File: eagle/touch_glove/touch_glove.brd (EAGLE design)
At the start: 160 x 100 mm, 0 parts

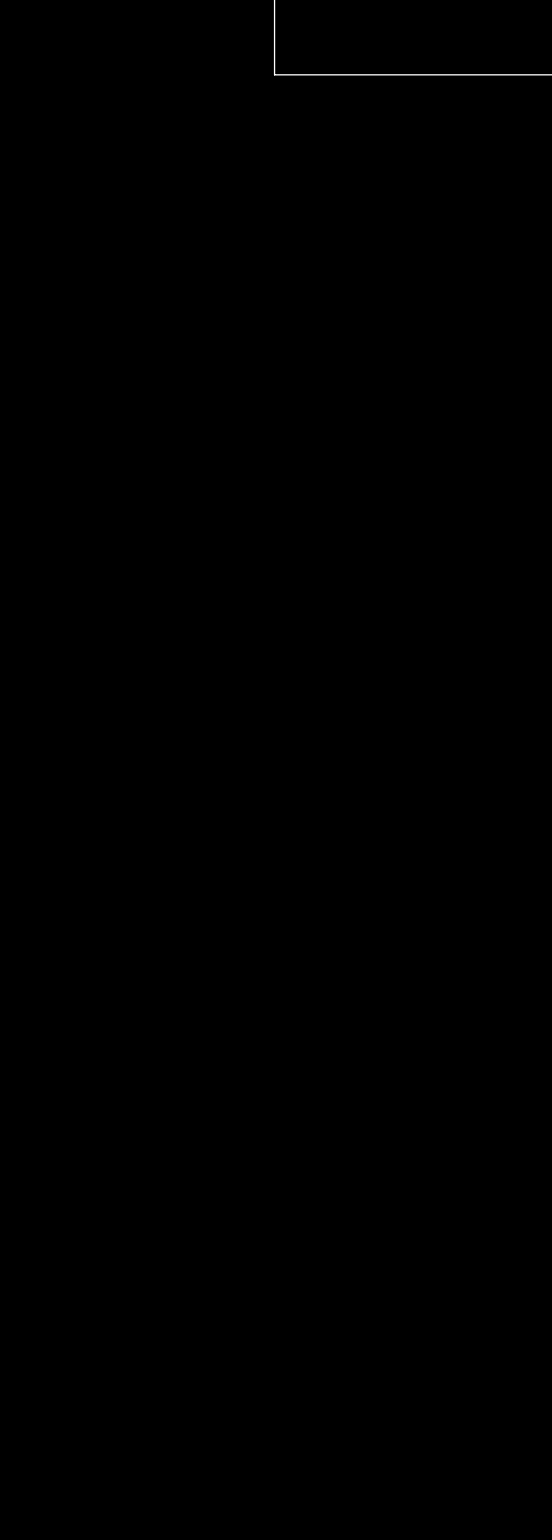
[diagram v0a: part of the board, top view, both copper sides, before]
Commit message: Added PWM driver and DEMUX to both robotic arm and touch glove.  Added some transistors to touch glove
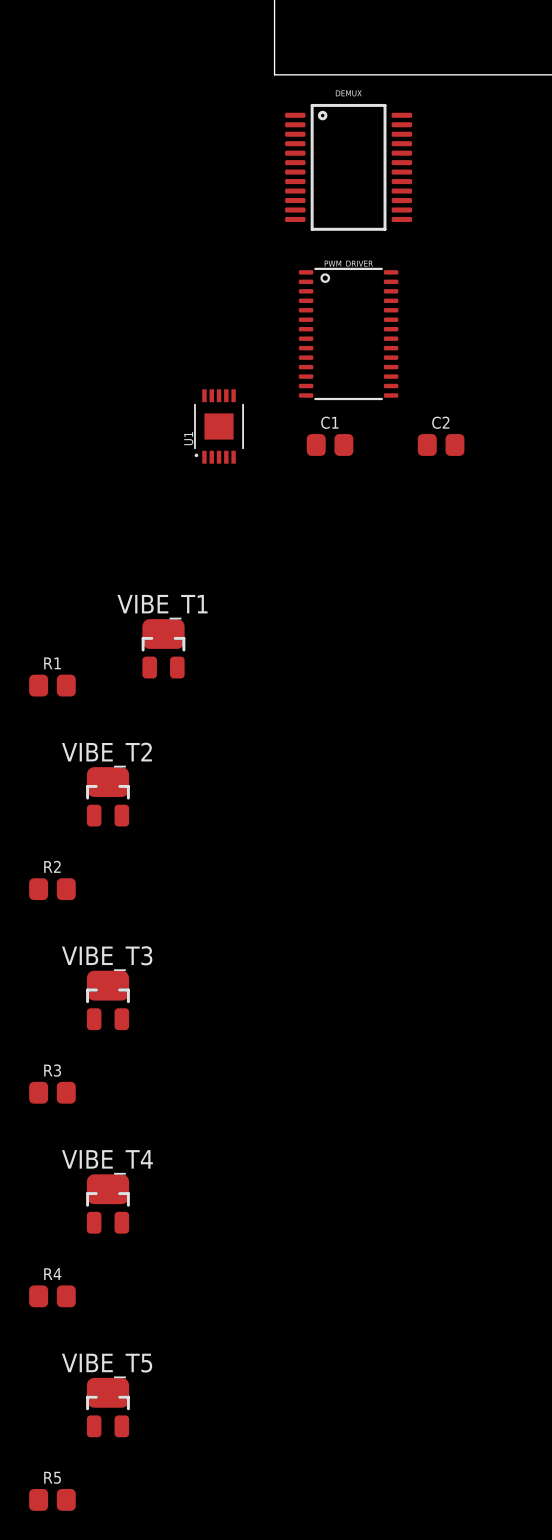
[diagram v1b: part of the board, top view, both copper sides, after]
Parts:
- added C1: CAP_CER_SMD-805_0.1UF-50V-10%, MrSwirlyEyes:CAP_CER_SMD-805_0.1UF-50V-10%
- added C2: CAP_CER_SMD-805_10UF-25V-10%, MrSwirlyEyes:CAP_CER_SMD-805_10UF-25V-10%
- added DEMUX: CD74HC4067-SM96_16:1_MUX-DEMUX, MrSwirlyEyes:SSOP24
- added PWM_DRIVER: PCA9685_16-CH_12-BIT_PWM-DRIVER, MrSwirlyEyes:TSSOP28
- added R1, R2, R3, R4, R5: RES_SMD-805_10K-5%-1/8W, MrSwirlyEyes:RES_SMD-805_10K-5%-1/8W
- added U1: DRV8830, SparkFun-Retired:MSOP-10-GNDPAD
- added VIBE_T1, VIBE_T2, VIBE_T3, VIBE_T4, VIBE_T5: SI2302CDS-MOSFET-N-CH_2.6A_20V_57MΩ_SOT23-3, MrSwirlyEyes:SOT23-3
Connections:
- new net C10: DEMUX.21
- new net C11: DEMUX.20
- new net C12: DEMUX.19
- new net C13: DEMUX.18
- new net C14: DEMUX.17
- new net C15: DEMUX.16
- new net C5: DEMUX.4
- new net C6: DEMUX.3
- new net C7: DEMUX.2
- new net C8: DEMUX.23
- new net C9: DEMUX.22
- new net GND: C1.2, C2.2, DEMUX.12, DEMUX.15, PWM_DRIVER.1, PWM_DRIVER.14, PWM_DRIVER.2, PWM_DRIVER.23, PWM_DRIVER.24, PWM_DRIVER.25, PWM_DRIVER.3, PWM_DRIVER.4, PWM_DRIVER.5, R1.1, R2.1, R3.1, R4.1, R5.1, U1.5, VIBE_T1.S, VIBE_T2.S, VIBE_T3.S, VIBE_T4.S, VIBE_T5.S
- new net OUT1: U1.3
- new net OUT2: U1.1
- new net PPAD: U1.GND
- new net PWM10: PWM_DRIVER.17
- new net S0: DEMUX.10
- new net S1: DEMUX.11
- new net S2: DEMUX.14
- new net S3: DEMUX.13
- new net SCL: PWM_DRIVER.26
- new net SDA: PWM_DRIVER.27
- new net SIG: DEMUX.1
- new net STRAIN_1: DEMUX.9
- new net STRAIN_2: DEMUX.8
- new net STRAIN_3: DEMUX.7
- new net STRAIN_4: DEMUX.6
- new net STRAIN_5: DEMUX.5
- new net TEC_1_COLD: PWM_DRIVER.7
- new net TEC_1_HOT: PWM_DRIVER.6
- new net TEC_2_COLD: PWM_DRIVER.9
- new net TEC_2_HOT: PWM_DRIVER.8
- new net TEC_3_COLD: PWM_DRIVER.11
- new net TEC_3_HOT: PWM_DRIVER.10
- new net TEC_4_COLD: PWM_DRIVER.13
- new net TEC_4_HOT: PWM_DRIVER.12
- new net TEC_5_COLD: PWM_DRIVER.16
- new net TEC_5_HOT: PWM_DRIVER.15
- new net VCC: C1.1, C2.1, DEMUX.24, PWM_DRIVER.28, U1.4, VIBE_T1.D, VIBE_T2.D, VIBE_T3.D, VIBE_T4.D, VIBE_T5.D
- new net VIBE_1: PWM_DRIVER.18, R1.2, VIBE_T1.G
- new net VIBE_2: PWM_DRIVER.19, R2.2, VIBE_T2.G
- new net VIBE_3: PWM_DRIVER.20, R3.2, VIBE_T3.G
- new net VIBE_4: PWM_DRIVER.21, R4.2, VIBE_T4.G
- new net VIBE_5: PWM_DRIVER.22, R5.2, VIBE_T5.G

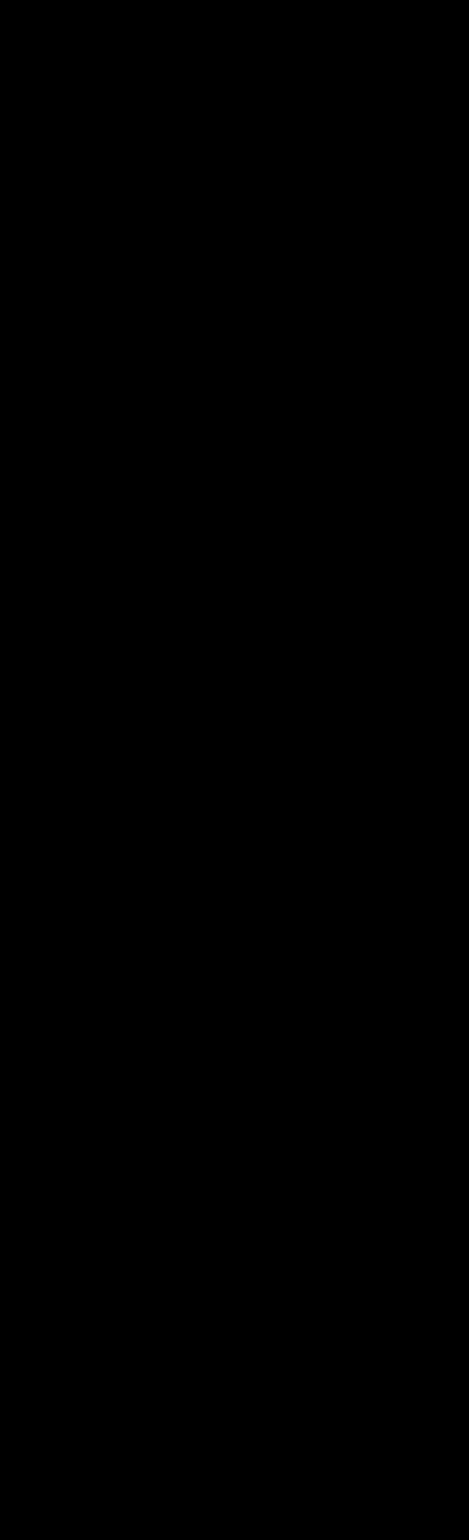
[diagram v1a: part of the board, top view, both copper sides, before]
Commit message: Added vibe motor plus transistor driver arrangement
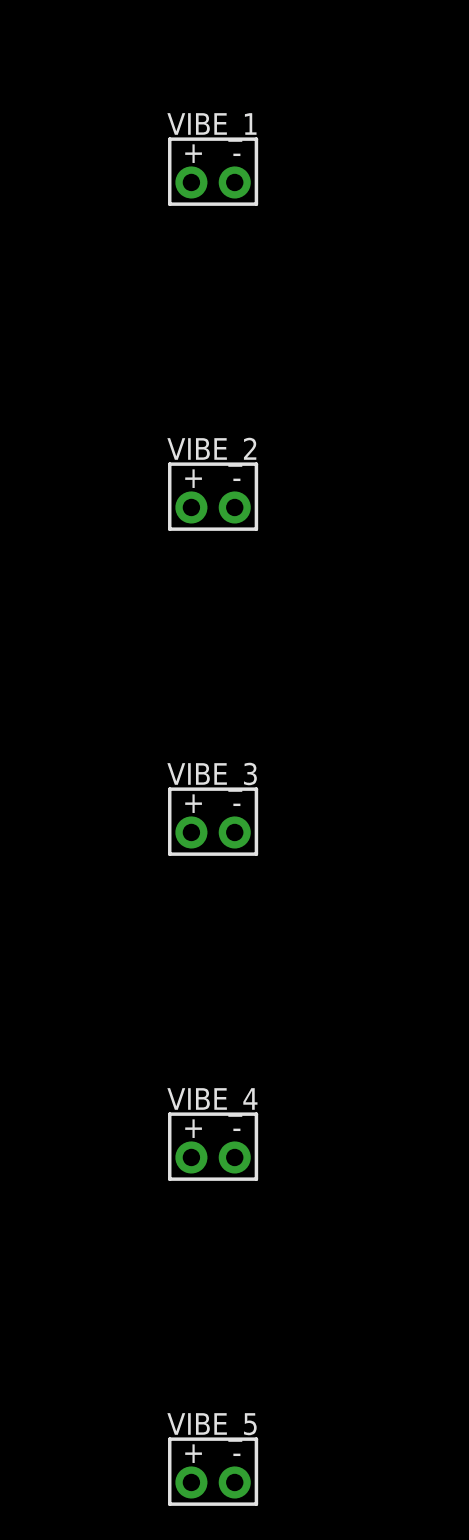
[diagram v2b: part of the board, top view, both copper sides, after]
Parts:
- added VIBE_1, VIBE_2, VIBE_3, VIBE_4, VIBE_5: VIBE_MOTOR, MrSwirlyEyes:CONNECTOR-01X02
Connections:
- new net N$1: VIBE_1.2, VIBE_T1.D
- new net N$2: VIBE_5.2, VIBE_T5.D
- new net N$3: VIBE_4.2, VIBE_T4.D
- new net N$4: VIBE_3.2, VIBE_T3.D
- new net N$5: VIBE_2.2, VIBE_T2.D
- net VCC: now also VIBE_1.1, VIBE_2.1, VIBE_3.1, VIBE_4.1, VIBE_5.1; no longer VIBE_T1.D, VIBE_T2.D, VIBE_T3.D, VIBE_T4.D, VIBE_T5.D
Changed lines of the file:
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@@
 <attribute name="TESTED" value="NO" x="-20.32" y="-92.71" size="1.778" layer="27" display="off"/>
+</element>
+<element name="VIBE_1" library="MrSwirlyEyes" package="CONNECTOR-01X02" value="VIBE_MOTOR" x="-6.35" y="-109.22">
+<attribute name="CREATOR" value="MrSwirlyEyes" x="-6.35" y="-109.22" size="1.778" layer="27" display="off"/>
+<attribute name="DATASHEET" value="http://www.vibration-motor.com/products/download/C0825B002F.pdf" x="-6.35" y="-109.22" size="1.778" layer="27" display="off"/>
+<attribute name="DIST" value="Digikey" x="-6.35" y="-109.22" size="1.778" layer="27" display="off"/>
+<attribute name="DISTPN" value="1670-1002-ND" x="-6.35" y="-109.22" size="1.778" layer="27" display="off"/>
+<attribute name="MFR" value="Jinlong Machinery &amp; Electronics, Inc." x="-6.35" y="-109.22" size="1.778" layer="27" display="off"/>
+<attribute name="MPN" value="C0825B002F" x="-6.35" y="-109.22" size="1.778" layer="27" display="off"/>
+<attribute name="TESTED" value="NO" x="-6.35" y="-109.22" size="1.778" layer="27" display="off"/>
+</element>
+<element name="VIBE_2" library="MrSwirlyEyes" package="CONNECTOR-01X02" value="VIBE_MOTOR" x="-6.35" y="-128.27">
+<attribute name="CREATOR" value="MrSwirlyEyes" x="-6.35" y="-128.27" size="1.778" layer="27" display="off"/>
+<attribute name="DATASHEET" value="http://www.vibration-motor.com/products/download/C0825B002F.pdf" x="-6.35" y="-128.27" size="1.778" layer="27" display="off"/>
+<attribute name="DIST" value="Digikey" x="-6.35" y="-128.27" size="1.778" layer="27" display="off"/>
+<attribute name="DISTPN" value="1670-1002-ND" x="-6.35" y="-128.27" size="1.778" layer="27" display="off"/>
+<attribute name="MFR" value="Jinlong Machinery &amp; Electronics, Inc." x="-6.35" y="-128.27" size="1.778" layer="27" display="off"/>
+<attribute name="MPN" value="C0825B002F" x="-6.35" y="-128.27" size="1.778" layer="27" display="off"/>
+<attribute name="TESTED" value="NO" x="-6.35" y="-128.27" size="1.778" layer="27" display="off"/>
+</element>
+<element name="VIBE_3" library="MrSwirlyEyes" package="CONNECTOR-01X02" value="VIBE_MOTOR" x="-6.35" y="-147.32">
+<attribute name="CREATOR" value="MrSwirlyEyes" x="-6.35" y="-147.32" size="1.778" layer="27" display="off"/>
+<attribute name="DATASHEET" value="http://www.vibration-motor.com/products/download/C0825B002F.pdf" x="-6.35" y="-147.32" size="1.778" layer="27" display="off"/>
+<attribute name="DIST" value="Digikey" x="-6.35" y="-147.32" size="1.778" layer="27" display="off"/>
+<attribute name="DISTPN" value="1670-1002-ND" x="-6.35" y="-147.32" size="1.778" layer="27" display="off"/>
+<attribute name="MFR" value="Jinlong Machinery &amp; Electronics, Inc." x="-6.35" y="-147.32" size="1.778" layer="27" display="off"/>
+<attribute name="MPN" value="C0825B002F" x="-6.35" y="-147.32" size="1.778" layer="27" display="off"/>
+<attribute name="TESTED" value="NO" x="-6.35" y="-147.32" size="1.778" layer="27" display="off"/>
+</element>
+<element name="VIBE_4" library="MrSwirlyEyes" package="CONNECTOR-01X02" value="VIBE_MOTOR" x="-6.35" y="-166.37">
+<attribute name="CREATOR" value="MrSwirlyEyes" x="-6.35" y="-166.37" size="1.778" layer="27" display="off"/>
+<attribute name="DATASHEET" value="http://www.vibration-motor.com/products/download/C0825B002F.pdf" x="-6.35" y="-166.37" size="1.778" layer="27" display="off"/>
+<attribute name="DIST" value="Digikey" x="-6.35" y="-166.37" size="1.778" layer="27" display="off"/>
+<attribute name="DISTPN" value="1670-1002-ND" x="-6.35" y="-166.37" size="1.778" layer="27" display="off"/>
+<attribute name="MFR" value="Jinlong Machinery &amp; Electronics, Inc." x="-6.35" y="-166.37" size="1.778" layer="27" display="off"/>
+<attribute name="MPN" value="C0825B002F" x="-6.35" y="-166.37" size="1.778" layer="27" display="off"/>
+<attribute name="TESTED" value="NO" x="-6.35" y="-166.37" size="1.778" layer="27" display="off"/>
+</element>
+<element name="VIBE_5" library="MrSwirlyEyes" package="CONNECTOR-01X02" value="VIBE_MOTOR" x="-6.35" y="-185.42">
+<attribute name="CREATOR" value="MrSwirlyEyes" x="-6.35" y="-185.42" size="1.778" layer="27" display="off"/>
+<attribute name="DATASHEET" value="http://www.vibration-motor.com/products/download/C0825B002F.pdf" x="-6.35" y="-185.42" size="1.778" layer="27" display="off"/>
+<attribute name="DIST" value="Digikey" x="-6.35" y="-185.42" size="1.778" layer="27" display="off"/>
+<attribute name="DISTPN" value="1670-1002-ND" x="-6.35" y="-185.42" size="1.778" layer="27" display="off"/>
+<attribute name="MFR" value="Jinlong Machinery &amp; Electronics, Inc." x="-6.35" y="-185.42" size="1.778" layer="27" display="off"/>
+<attribute name="MPN" value="C0825B002F" x="-6.35" y="-185.42" size="1.778" layer="27" display="off"/>
+<attribute name="TESTED" value="NO" x="-6.35" y="-185.42" size="1.778" layer="27" display="off"/>
 </element>
 </elements>
@@
 <contactref element="PWM_DRIVER" pad="28"/>
 <contactref element="C2" pad="1"/>
-<contactref element="VIBE_T1" pad="D"/>
-<contactref element="VIBE_T2" pad="D"/>
-<contactref element="VIBE_T3" pad="D"/>
-<contactref element="VIBE_T4" pad="D"/>
-<contactref element="VIBE_T5" pad="D"/>
-<wire x1="-11.43" y1="-76.47" x2="-11.43" y2="-90.44" width="0" layer="19" extent="1-1"/>
-<wire x1="-11.43" y1="-62.5" x2="-11.43" y2="-76.47" width="0" layer="19" extent="1-1"/>
-<wire x1="-11.43" y1="-48.53" x2="-11.43" y2="-62.5" width="0" layer="19" extent="1-1"/>
-<wire x1="-7.62" y1="-38.37" x2="-11.43" y2="-48.53" width="0" layer="19" extent="1-1"/>
-<wire x1="-3.31" y1="-26.2395" x2="-7.62" y2="-38.37" width="0" layer="19" extent="1-1"/>
+<contactref element="VIBE_1" pad="1"/>
+<contactref element="VIBE_5" pad="1"/>
+<contactref element="VIBE_4" pad="1"/>
+<contactref element="VIBE_3" pad="1"/>
+<contactref element="VIBE_2" pad="1"/>
+<wire x1="-7.62" y1="-167.64" x2="-7.62" y2="-186.69" width="0" layer="19" extent="1-1"/>
+<wire x1="-7.62" y1="-148.59" x2="-7.62" y2="-167.64" width="0" layer="19" extent="1-1"/>
+<wire x1="-7.62" y1="-129.54" x2="-7.62" y2="-148.59" width="0" layer="19" extent="1-1"/>
+<wire x1="-7.62" y1="-110.49" x2="-7.62" y2="-129.54" width="0" layer="19" extent="1-1"/>
+<wire x1="-3.31" y1="-26.2395" x2="-7.62" y2="-110.49" width="0" layer="19" extent="1-1"/>
 <wire x1="2.86" y1="-25.4" x2="-3.31" y2="-26.2395" width="0" layer="19" extent="1-1"/>
 <wire x1="10.48" y1="-25.4" x2="2.86" y2="-25.4" width="0" layer="19" extent="1-1"/>
@@
 <contactref element="U1" pad="GND"/>
 </signal>
+<signal name="N$1">
+<contactref element="VIBE_T1" pad="D"/>
+<contactref element="VIBE_1" pad="2"/>
+<wire x1="-7.62" y1="-38.37" x2="-5.08" y2="-110.49" width="0" layer="19" extent="1-1"/>
+</signal>
+<signal name="N$2">
+<contactref element="VIBE_5" pad="2"/>
+<contactref element="VIBE_T5" pad="D"/>
+<wire x1="-11.43" y1="-90.44" x2="-5.08" y2="-186.69" width="0" layer="19" extent="1-1"/>
+</signal>
+<signal name="N$3">
+<contactref element="VIBE_T4" pad="D"/>
+<contactref element="VIBE_4" pad="2"/>
+<wire x1="-11.43" y1="-76.47" x2="-5.08" y2="-167.64" width="0" layer="19" extent="1-1"/>
+</signal>
+<signal name="N$4">
+<contactref element="VIBE_T3" pad="D"/>
+<contactref element="VIBE_3" pad="2"/>
+<wire x1="-11.43" y1="-62.5" x2="-5.08" y2="-148.59" width="0" layer="19" extent="1-1"/>
+</signal>
+<signal name="N$5">
+<contactref element="VIBE_2" pad="2"/>
+<contactref element="VIBE_T2" pad="D"/>
+<wire x1="-11.43" y1="-48.53" x2="-5.08" y2="-129.54" width="0" layer="19" extent="1-1"/>
+</signal>
 </signals>

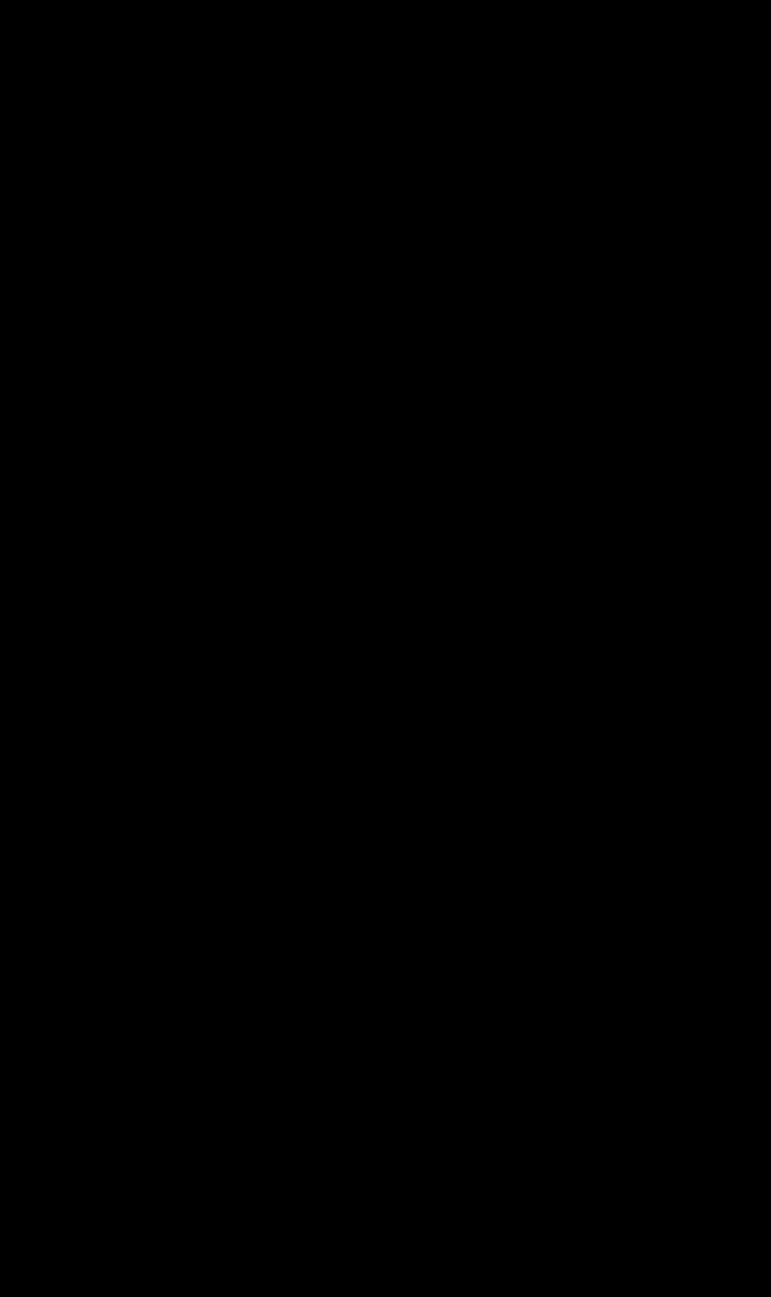
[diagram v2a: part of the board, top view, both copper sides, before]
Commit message: Added diode and cap to Touch Glove vibe motor drivers
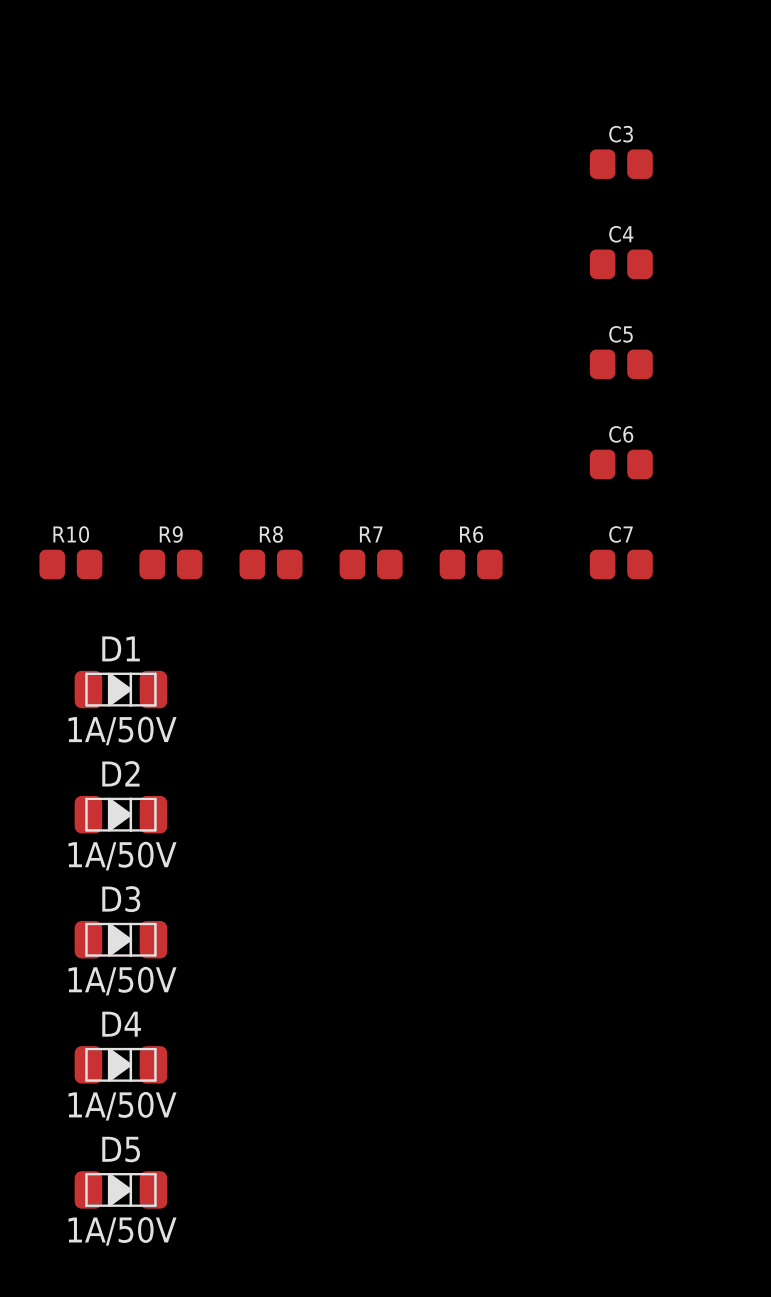
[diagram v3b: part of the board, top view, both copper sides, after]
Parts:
- added C3, C4, C5, C6, C7: CAP_CER_SMD-805_0.1UF-50V-10%, MrSwirlyEyes:CAP_CER_SMD-805_0.1UF-50V-10%
- added D1, D2, D3, D4, D5: DIODE_SMD_GP_1A-50V-SOD123F, MrSwirlyEyes:DIODE_SMD_1A-50V-SOD123F
- added R10, R6, R7, R8, R9: RES_SMD-805_10K-5%-1/8W, MrSwirlyEyes:RES_SMD-805_10K-5%-1/8W
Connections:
- removed net N$2: VIBE_5.2, VIBE_T5.D
- removed net N$5: VIBE_2.2, VIBE_T2.D
- new net N$10: R7.1
- new net N$11: C4.2, D2.A, VIBE_2.2, VIBE_T2.D
- new net N$14: C7.2, D5.A, VIBE_5.2, VIBE_T5.D
- new net N$6: R6.1
- new net N$7: R10.1
- new net N$8: R9.1
- new net N$9: R8.1
- net N$1: now also C3.2, D1.A
- net N$3: now also C6.2, D4.A
- net N$4: now also C5.2, D3.A
- net VCC: now also C3.1, C4.1, C5.1, C6.1, C7.1, D1.K, D2.K, D3.K, D4.K, D5.K
- net VIBE_1: now also R6.2
- net VIBE_2: now also R7.2
- net VIBE_3: now also R8.2
- net VIBE_4: now also R9.2
- net VIBE_5: now also R10.2
